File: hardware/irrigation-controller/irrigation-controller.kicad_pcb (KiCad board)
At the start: 2 copper layers, 109 x 71.6 mm, 83 parts, among them J1 RS485, J10 I2C, J11 IO, J12 RELAY_2, J15 FLOW_1, J2 I2C, J3 ICSP, J4 UART, J5 RF Module, J6 PWR 24V, J7 RELAY_1, J8 RELAY_3, J9 RELAY_4, K1 RELAY_3, K2 RELAY_4, Q1 MMBT3904, Q2 MMBT3904, Q3 2N7002, Q4 2N7002, Q5 2N7002, Q6 2N7002, SW1 RESET, SW2 BUTTON, U1 AQY280EH, U2 ATmega328P-AU, U3 AQY280EH, U4 TPS54331DR, U5 TPS54331DR, U6 MAX485, Y1 8MHz

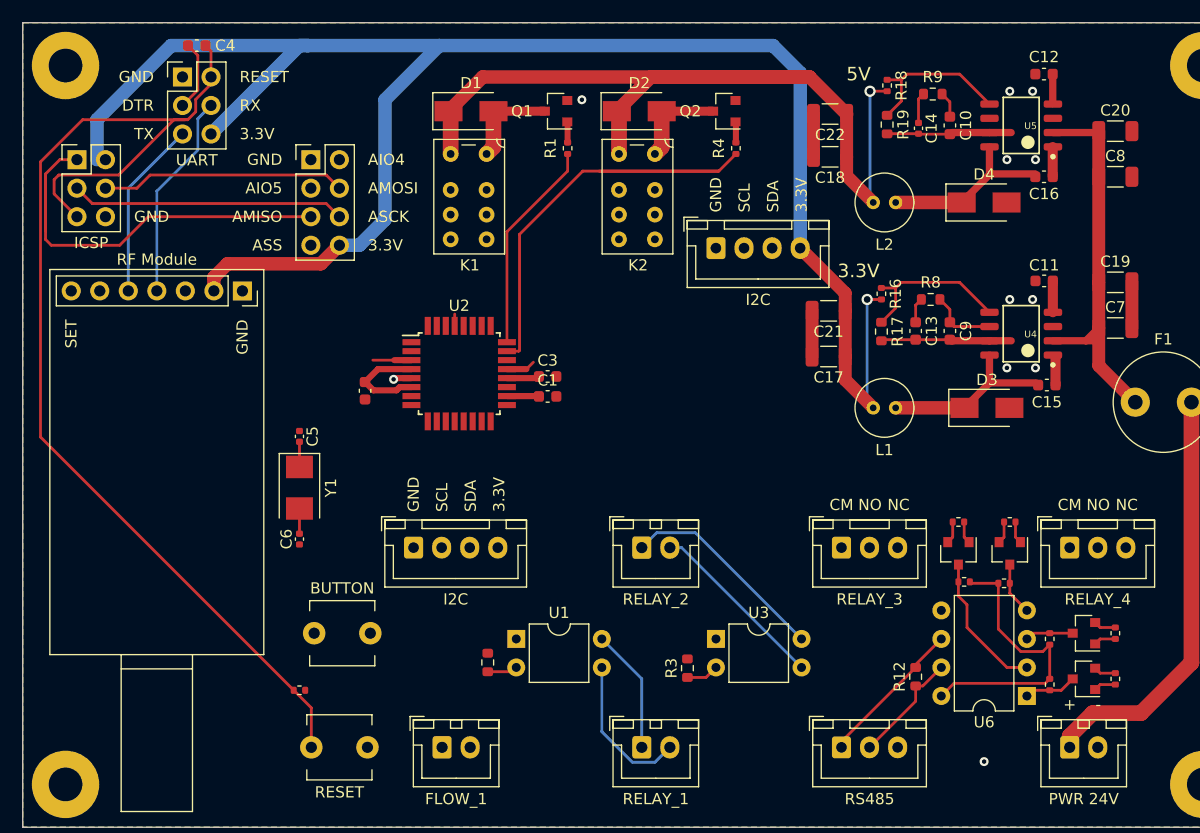
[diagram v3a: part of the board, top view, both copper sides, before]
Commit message: Route all controller board nets
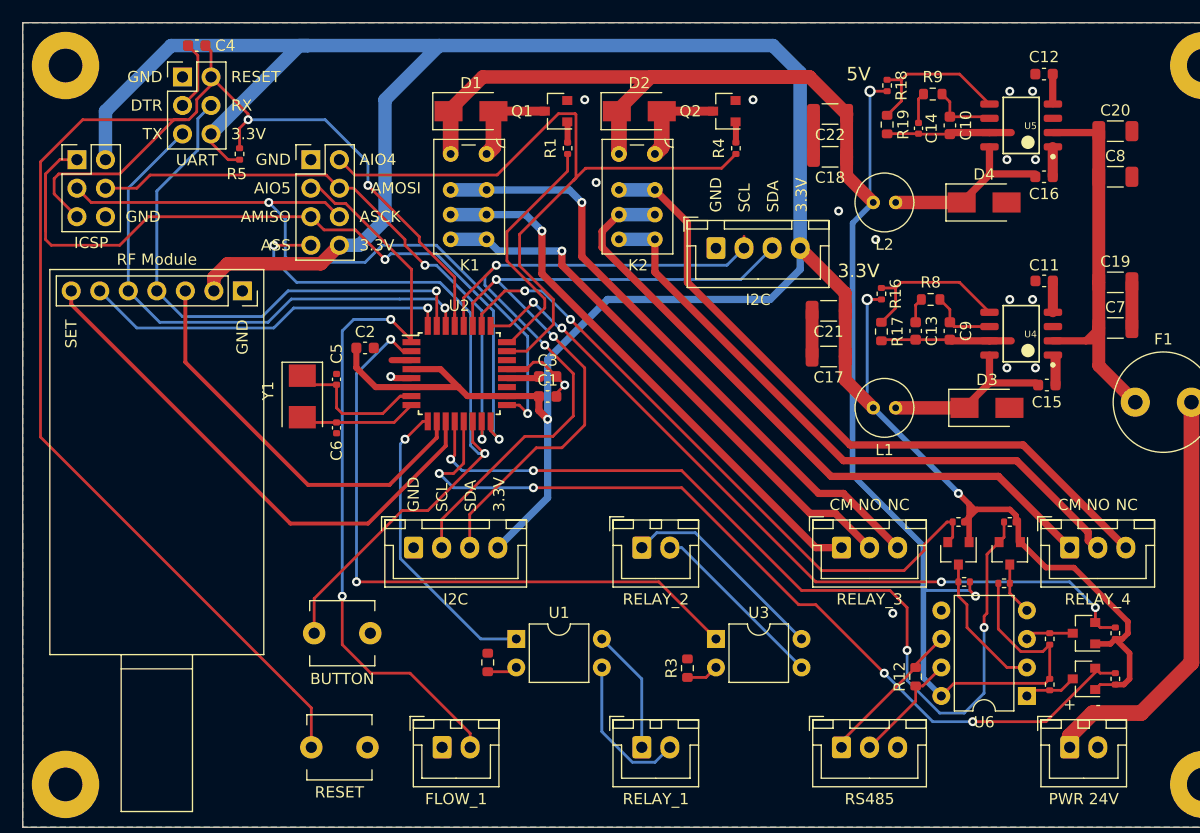
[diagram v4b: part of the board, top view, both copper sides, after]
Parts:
- moved R5 48.0 mm to (70.9, 89.4), turned to 90 degrees
- moved C6 10.4 mm to (79.5, 113.8)
- moved Y1 8.13 mm to (76.5, 111.0)
- moved C5 6.06 mm to (79.5, 109.5)
- moved C2 3.81 mm to (82.0, 106.7), turned to 0 degrees
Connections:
- K1 pad 5: R3BNO -> R3ANO
- K1 pad 6: R3BC -> R3AC
- K1 pad 7: R3BNC -> R3ANC
- K2 pad 5: R4BNO -> R4ANO
- K2 pad 6: R4BC -> R4AC
- K2 pad 7: R4BNC -> R4ANC
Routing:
- net +3V3: track 182.0 -> 286.7 mm, vias 1 -> 3
- net ASTX: track 1.98 -> 80.9 mm, vias 0 -> 4
- net ASRX: track 1.98 -> 78.0 mm, vias 0 -> 4
- net AIO5: track 0.00 -> 69.8 mm, vias 0 -> 2
- net ARSDE: track 1.98 -> 69.3 mm, vias 0 -> 4
- net ASCL: track 0.00 -> 65.5 mm, vias 0 -> 2
- net ASS: track 0.00 -> 64.4 mm, vias 0 -> 2
- net ASDA: track 0.00 -> 63.4 mm, vias 0 -> 2
- net R4ANC: track 0.00 -> 61.5 mm
- net R4AC: track 0.00 -> 59.4 mm
- net AIO2: track 0.00 -> 59.2 mm, vias 0 -> 2
- net ARSRE: track 1.98 -> 58.2 mm, vias 0 -> 2
- net R4ANO: track 0.00 -> 56.1 mm
- net R3ANC: track 0.00 -> 55.8 mm, vias 0 -> 1
- net +5V: track 110.3 -> 162.4 mm, vias 1 -> 2
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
